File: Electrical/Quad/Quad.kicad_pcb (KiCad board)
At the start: 2 copper layers, 140 x 70 mm, 133 parts, among them J101 01x04, J102 01x04, J103 01x03, J104 01x03, J201 01x03, J202 01x04, J203 01x03, J204 01x04, J205 01x03, J206 USB_OTG, J207 01x04, J208 01x02, J209 01x04, J210 01x02, J211 01x02, J212 4PostTerm, J213 2PostTerm, J214 2PostTerm, J215 2PostTerm, J216 2PostTerm, J217 2PostTerm, J218 01x02, J219 01x02, Q201 FDC6420C, Q202 FDG1024NZ, Q301 FDC6420C, Q401 FDC6420C, Q501 FDC6420C, Q601 FDC6420C, U201 TPD4S012, U202 ACS723LLCTR-05AB-T, U203 ACS723LLCTR-05AB-T, U204 24LC256, U205 LM2576HVS-ADJ, U206 LM2576HVS-ADJ

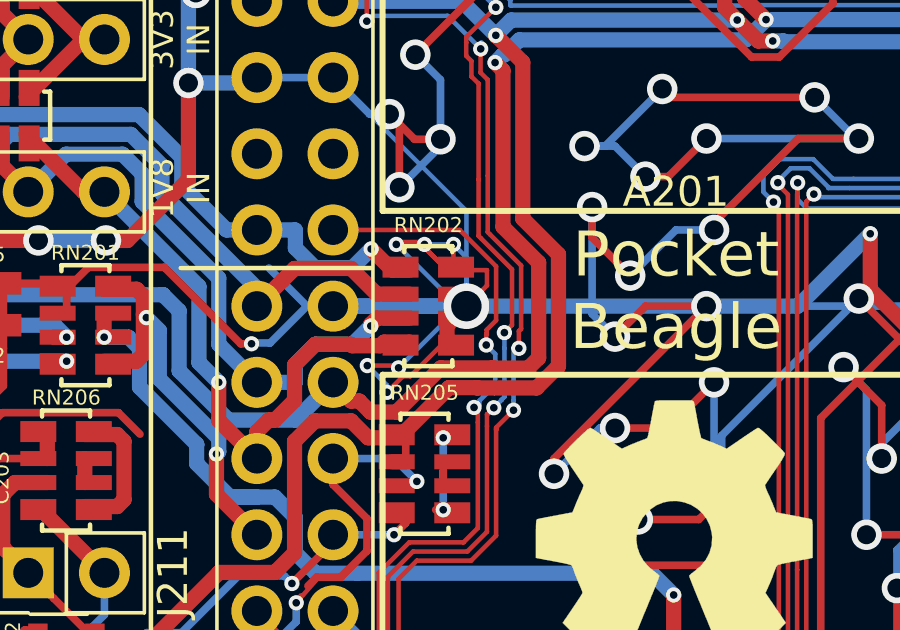
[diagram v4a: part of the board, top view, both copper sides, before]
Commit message: Modified ground viaing for better soldering.
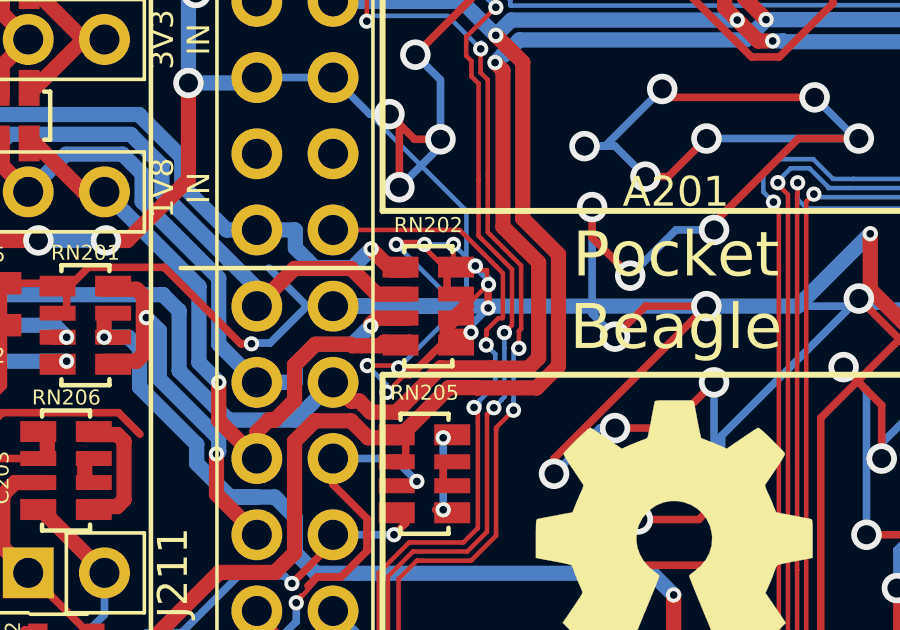
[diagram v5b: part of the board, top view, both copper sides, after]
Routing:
- net GND: track 2545.8 -> 2553.1 mm, vias 409 -> 412
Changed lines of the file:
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@@
     (thickness 1.6)
     (drawings 208)
-    (tracks 5484)
+    (tracks 5503)
     (zones 0)
     (modules 133)
@@
   (segment (start 55.7024 87.5032) (end 55.4738 87.7318) (width 0.254) (layer B.Cu) (net 0))
   (via (at 59.4362 88.7732) (size 1.524) (drill 1.016) (layers F.Cu B.Cu) (net 0))
+  (segment (start 92.37 94.99) (end 92.37 95.79) (width 0.254) (layer F.Cu) (net 1))
+  (segment (start 93.313087 94.850513) (end 92.509487 94.850513) (width 0.254) (layer F.Cu) (net 1))
+  (segment (start 92.509487 94.850513) (end 92.37 94.99) (width 0.254) (layer F.Cu) (net 1))
+  (segment (start 93.752926 95.469566) (end 93.752926 95.290352) (width 0.254) (layer B.Cu) (net 1))
+  (segment (start 93.752926 95.290352) (end 93.313087 94.850513) (width 0.254) (layer B.Cu) (net 1))
+  (via (at 93.313087 94.850513) (size 0.508) (drill 0.254) (layers F.Cu B.Cu) (net 1))
+  (segment (start 93.739714 96.252467) (end 93.739714 95.482778) (width 0.254) (layer F.Cu) (net 1))
+  (segment (start 93.739714 95.482778) (end 93.752926 95.469566) (width 0.254) (layer F.Cu) (net 1))
+  (via (at 93.752926 95.469566) (size 0.508) (drill 0.254) (layers F.Cu B.Cu) (net 1))
+  (segment (start 93.170339 97.065063) (end 93.170339 96.821842) (width 0.254) (layer B.Cu) (net 1))
+  (segment (start 93.170339 96.821842) (end 93.739714 96.252467) (width 0.254) (layer B.Cu) (net 1))
+  (via (at 93.739714 96.252467) (size 0.508) (drill 0.254) (layers F.Cu B.Cu) (net 1))
+  (segment (start 90.7544 98.246402) (end 91.408354 98.246402) (width 0.254) (layer F.Cu) (net 1))
+  (via (at 93.170339 97.065063) (size 0.508) (drill 0.254) (layers F.Cu B.Cu) (net 1))
+  (segment (start 91.408354 98.246402) (end 92.589693 97.065063) (width 0.254) (layer F.Cu) (net 1))
+  (segment (start 92.589693 97.065063) (end 93.170339 97.065063) (width 0.254) (layer F.Cu) (net 1))
   (segment (start 75.681146 68.25) (end 75.681146 68.60921) (width 0.254) (layer F.Cu) (net 1))
   (segment (start 75.681146 68.60921) (end 75.84 68.768064) (width 0.254) (layer F.Cu) (net 1))
@@
   (via (at 155.88 66.218) (size 1.016) (drill 0.635) (layers F.Cu B.Cu) (net 1))
   (via (at 153.34 66.218) (size 1.016) (drill 0.635) (layers F.Cu B.Cu) (net 1))
-  (via (at 93.015 96.19) (size 1.524) (drill 1.016) (layers F.Cu B.Cu) (net 1))
   (via (at 151.054 66.218) (size 1.016) (drill 0.635) (layers F.Cu B.Cu) (net 1))
   (via (at 168.072 122.352) (size 1.016) (drill 0.635) (layers F.Cu B.Cu) (net 1))
@@
   (segment (start 135.632036 127.686) (end 137.156036 126.162) (width 1.524) (layer B.Cu) (net 45))
   (segment (start 127.94 129.21) (end 129.464 127.686) (width 1.524) (layer B.Cu) (net 45))
+  (segment (start 88.57 93.65) (end 92.791482 93.65) (width 0.1524) (layer F.Cu) (net 46))
+  (segment (start 92.791482 93.65) (end 94.005601 94.864119) (width 0.1524) (layer F.Cu) (net 46))
+  (segment (start 94.078818 96.592272) (end 93.690346 96.980744) (width 0.1524) (layer F.Cu) (net 46))
+  (segment (start 94.005601 94.864119) (end 94.005601 94.869201) (width 0.1524) (layer F.Cu) (net 46))
+  (segment (start 94.005601 94.869201) (end 94.232986 95.096586) (width 0.1524) (layer F.Cu) (net 46))
+  (segment (start 94.212928 96.592272) (end 94.078818 96.592272) (width 0.1524) (layer F.Cu) (net 46))
+  (segment (start 94.232986 95.096586) (end 94.232986 96.572214) (width 0.1524) (layer F.Cu) (net 46))
+  (segment (start 93.690346 96.980744) (end 93.690346 97.112246) (width 0.1524) (layer F.Cu) (net 46))
+  (segment (start 94.232986 96.572214) (end 94.212928 96.592272) (width 0.1524) (layer F.Cu) (net 46))
+  (segment (start 93.690346 97.112246) (end 93.676402 97.12619) (width 0.1524) (layer F.Cu) (net 46))
+  (segment (start 93.676402 97.12619) (end 93.676402 97.4854) (width 0.1524) (layer F.Cu) (net 46))
   (segment (start 138.050547 132.996938) (end 138.050547 131.316853) (width 0.1524) (layer F.Cu) (net 46))
   (segment (start 138.050547 131.316853) (end 138.266399 131.101001) (width 0.1524) (layer F.Cu) (net 46))
@@
   (segment (start 130.48 131.47421) (end 130.48 131.115) (width 0.1524) (layer B.Cu) (net 46))
   (via (at 113.028885 131.382265) (size 0.508) (drill 0.254) (layers F.Cu B.Cu) (net 46))
-  (segment (start 88.57 93.65) (end 92.791482 93.65) (width 0.1524) (layer F.Cu) (net 46))
-  (segment (start 92.791482 93.65) (end 94.005601 94.864119) (width 0.1524) (layer F.Cu) (net 46))
-  (segment (start 94.005601 94.864119) (end 94.005601 96.665489) (width 0.1524) (layer F.Cu) (net 46))
-  (segment (start 94.005601 96.665489) (end 93.690346 96.980744) (width 0.1524) (layer F.Cu) (net 46))
-  (segment (start 93.690346 96.980744) (end 93.690346 97.112246) (width 0.1524) (layer F.Cu) (net 46))
-  (segment (start 93.690346 97.112246) (end 93.676402 97.12619) (width 0.1524) (layer F.Cu) (net 46))
-  (segment (start 93.676402 97.12619) (end 93.676402 97.4854) (width 0.1524) (layer F.Cu) (net 46))
   (segment (start 93.976447 99.063953) (end 93.976447 97.785445) (width 0.1524) (layer B.Cu) (net 46))
   (segment (start 93.976447 97.785445) (end 93.676402 97.4854) (width 0.1524) (layer B.Cu) (net 46))
